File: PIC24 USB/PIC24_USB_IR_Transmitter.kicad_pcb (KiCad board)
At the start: 2 copper layers, 18 parts, among them CON1 USB-MINI-B, U1 PIC24FJXXXGB106, X1 12Mhz

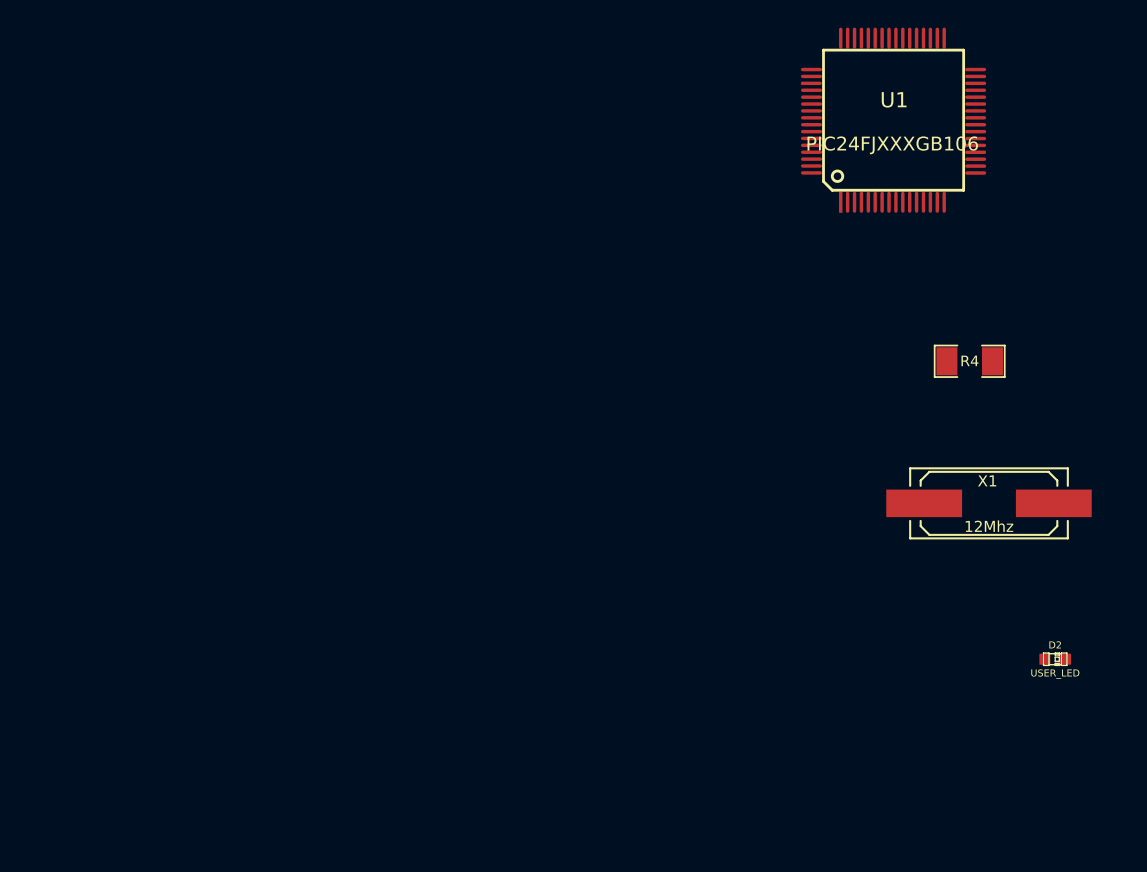
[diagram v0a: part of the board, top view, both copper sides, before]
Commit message: inserted regulator for +3v3
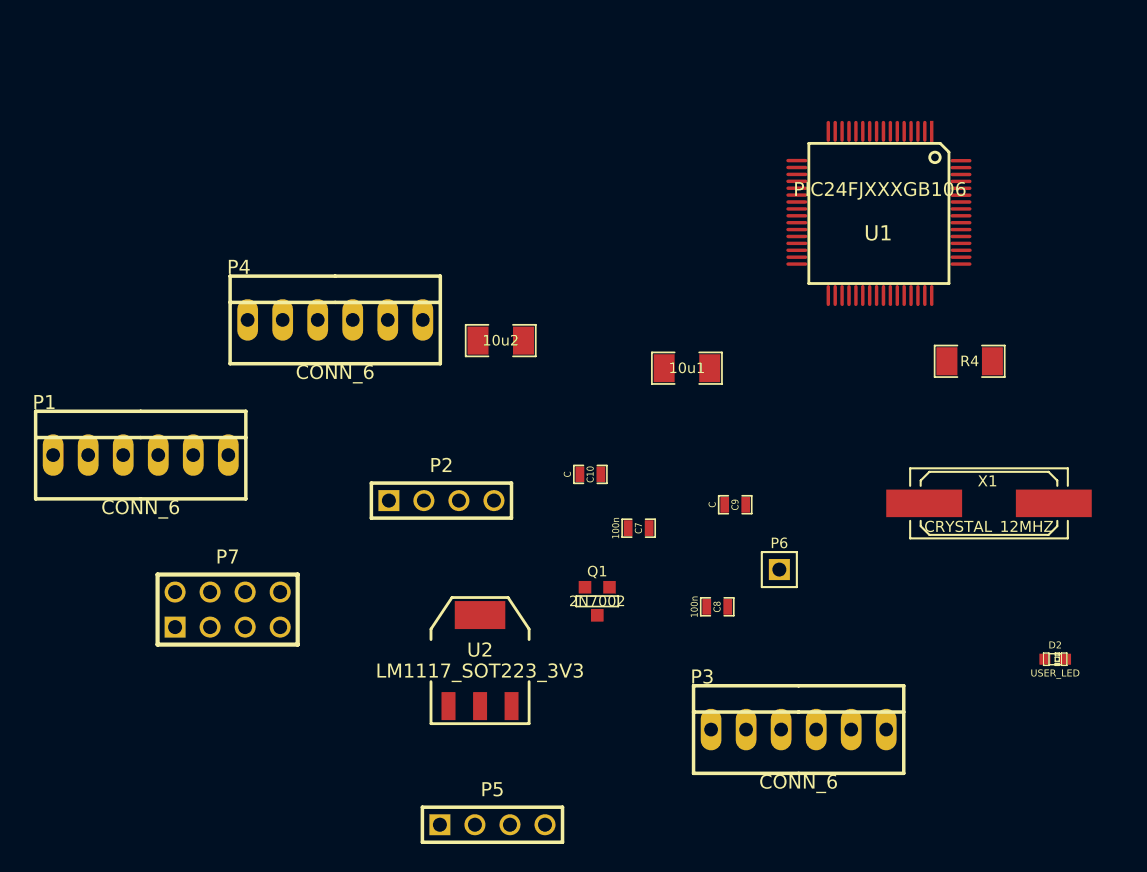
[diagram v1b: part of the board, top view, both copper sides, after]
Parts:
- added 10u1: C, SM1206, F.Cu at (105.8, 75.2)
- added 10u2: C, SM1206, F.Cu at (92.3, 73.2)
- added C10: C, SM0603_Capa, F.Cu at (98.8, 82.9)
- added C7: 100n, SM0603_Capa, F.Cu at (102.3, 86.8)
- added C8: 100n, SM0603_Capa, F.Cu at (108.0, 92.5)
- added C9: C, SM0603_Capa, F.Cu at (109.3, 85.1)
- added P1: CONN_6, PINHEAD1-6, F.Cu at (66.2, 81.5)
- added P2: CONN_4, PIN_ARRAY_4x1, F.Cu at (88.0, 84.8)
- added P3: CONN_6, PINHEAD1-6, F.Cu at (113.9, 101.4)
- added P4: CONN_6, PINHEAD1-6, F.Cu at (80.3, 71.7)
- added P5: CONN_4, PIN_ARRAY_4x1, F.Cu at (91.7, 108.3)
- added P6: CONN_1, PIN_ARRAY_1, F.Cu at (112.5, 89.8)
- added P7: CONN_8, pin_array_4x2, F.Cu at (72.5, 92.7)
- added Q1: 2N7002, SOT23GDS, F.Cu at (99.3, 92.1)
- added U2: LM1117_SOT223_3V3, SOT223, F.Cu at (90.8, 96.4)
- C3, C4: value 22p -> 100n
- X1: value 12Mhz -> CRYSTAL_12MHZ
- moved U1 6.66 mm to (119.8, 63.9), turned to 180 degrees
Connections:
- C3 pad 1: /OSC2 -> GND
- C3 pad 2: GND -> +3.3V
- C4 pad 1: /OSC1 -> GND
- C4 pad 2: GND -> +3.3V
- U1 pad 39: (no net) -> N-0000070
- U1 pad 40: (no net) -> N-0000069
- U1 pad 56: (no net) -> N-0000042
- U1 pad 57: (no net) -> +3.3V
- U1 pad 7: (no net) -> ~MCLR~
- X1 pad 1: /OSC1 -> N-0000069
- X1 pad 2: /OSC2 -> N-0000070

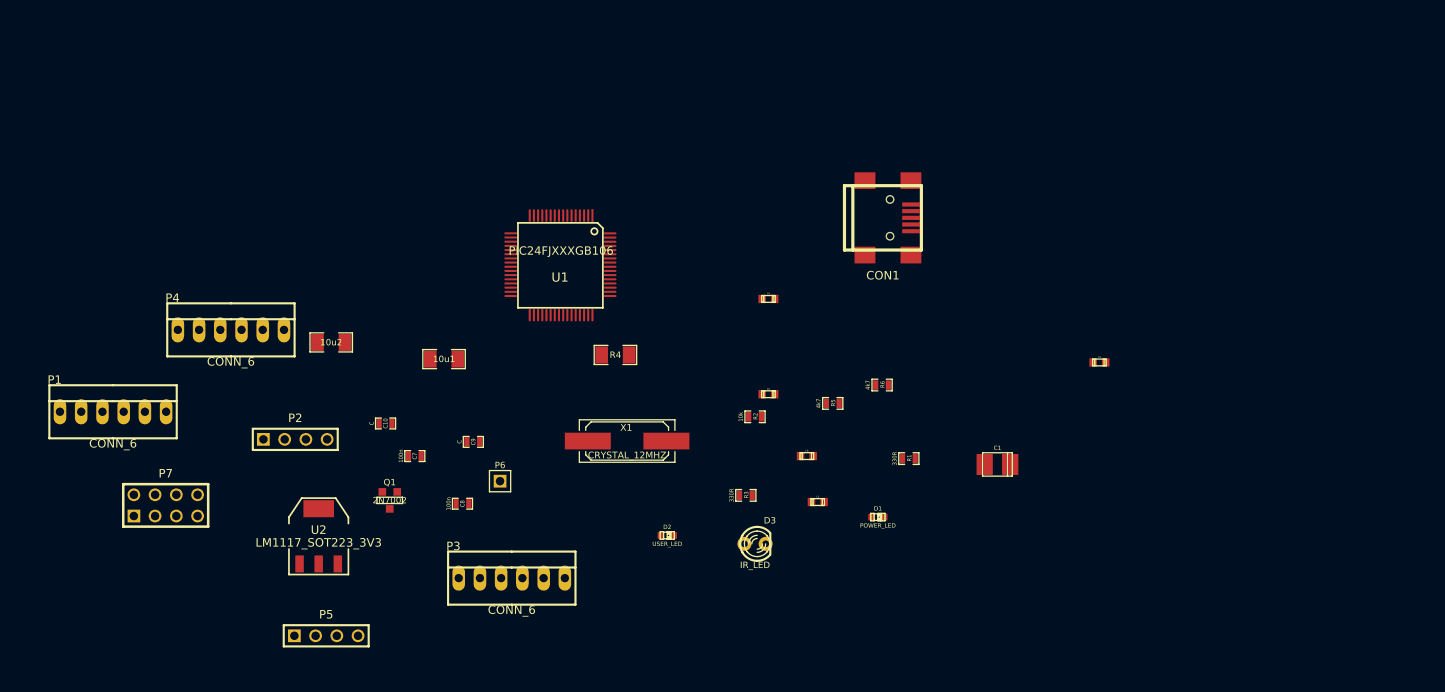
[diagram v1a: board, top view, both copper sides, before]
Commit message: inserted some mandatory mcu connecrtion and a bus connection
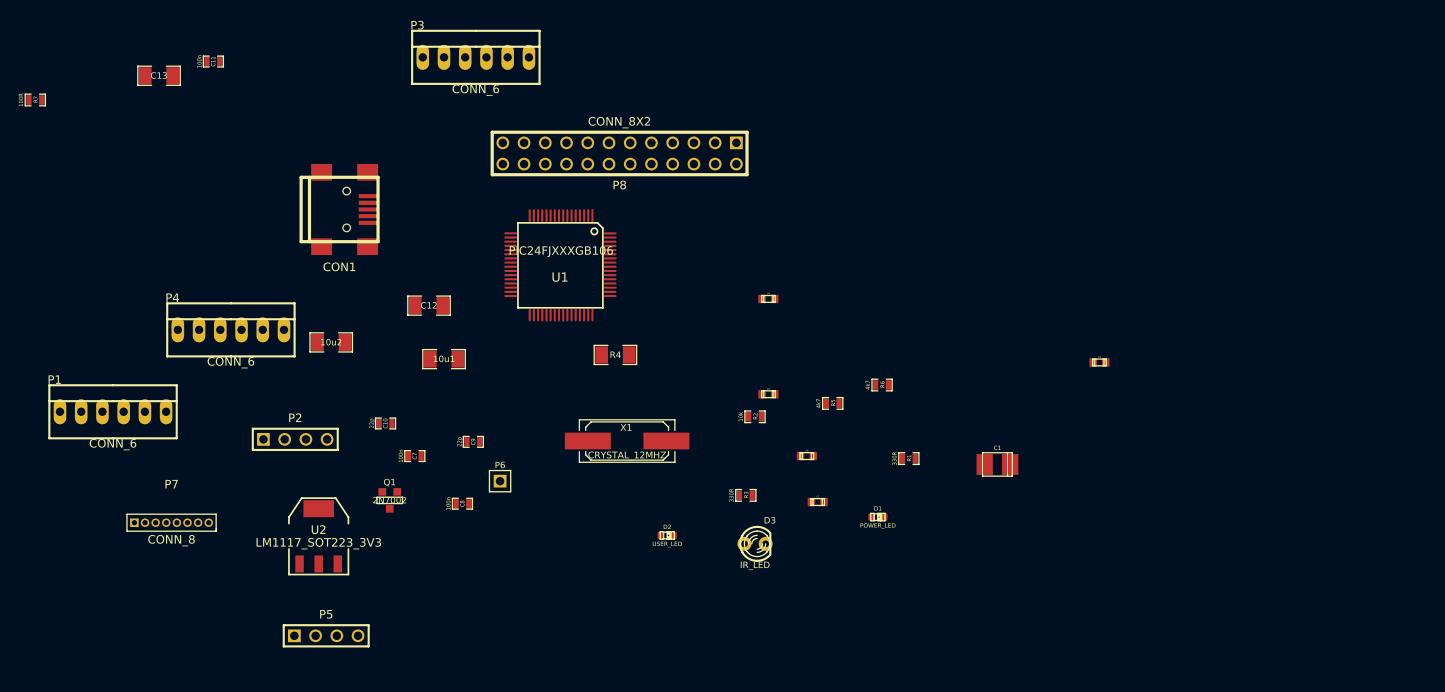
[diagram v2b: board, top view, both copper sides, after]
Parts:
- added C11: 100n, SM0603_Capa, F.Cu at (78.2, 39.6)
- added C12: 10u, SM1206, F.Cu at (104.0, 68.8)
- added C13: 10u, SM1206, F.Cu at (71.7, 41.3)
- added P8: CONN_8X2, pin_array_12x2, F.Cu at (126.8, 50.6)
- added R7: 100R, SM0603_Resistor, F.Cu at (56.9, 44.2)
- C10, C9: value C -> 22p
- P7: footprint pin_array_4x2 -> pin_array_8_50mil
- moved CON1 65.0 mm to (93.3, 57.3)
- moved P3 62.4 mm to (109.6, 39.1)
- moved P7 1.06 mm to (73.2, 93.5)
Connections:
- 10u2 pad 2: N-0000042 (its old number) -> N-0000050
- P1 pad 2: +5V -> +3.3V
- P1 pad 4: (no net) -> PGD
- P1 pad 5: (no net) -> PGC
- R2 pad 1: +5V -> ~MCLR~
- R2 pad 2: ~MCLR~ -> +3.3V
- U1 pad 1: (no net) -> /RE5
- U1 pad 17: (no net) -> PGC
- U1 pad 18: (no net) -> PGD
- U1 pad 2: (no net) -> /RE6
- U1 pad 3: (no net) -> /RE7
- U1 pad 43: (no net) -> SDA
- U1 pad 44: (no net) -> SCL
- U1 pad 56: N-0000042 (its old number) -> N-0000066
- U1 pad 60: (no net) -> /RE0
- U1 pad 61: (no net) -> /RE1
- U1 pad 62: (no net) -> /RE2
- U1 pad 63: (no net) -> /RE3
- U1 pad 64: (no net) -> /RE4
- U1 pad 7: ~MCLR~ -> N-0000072

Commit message: converted kicad project for newer version from kicad.nosoftware.cz
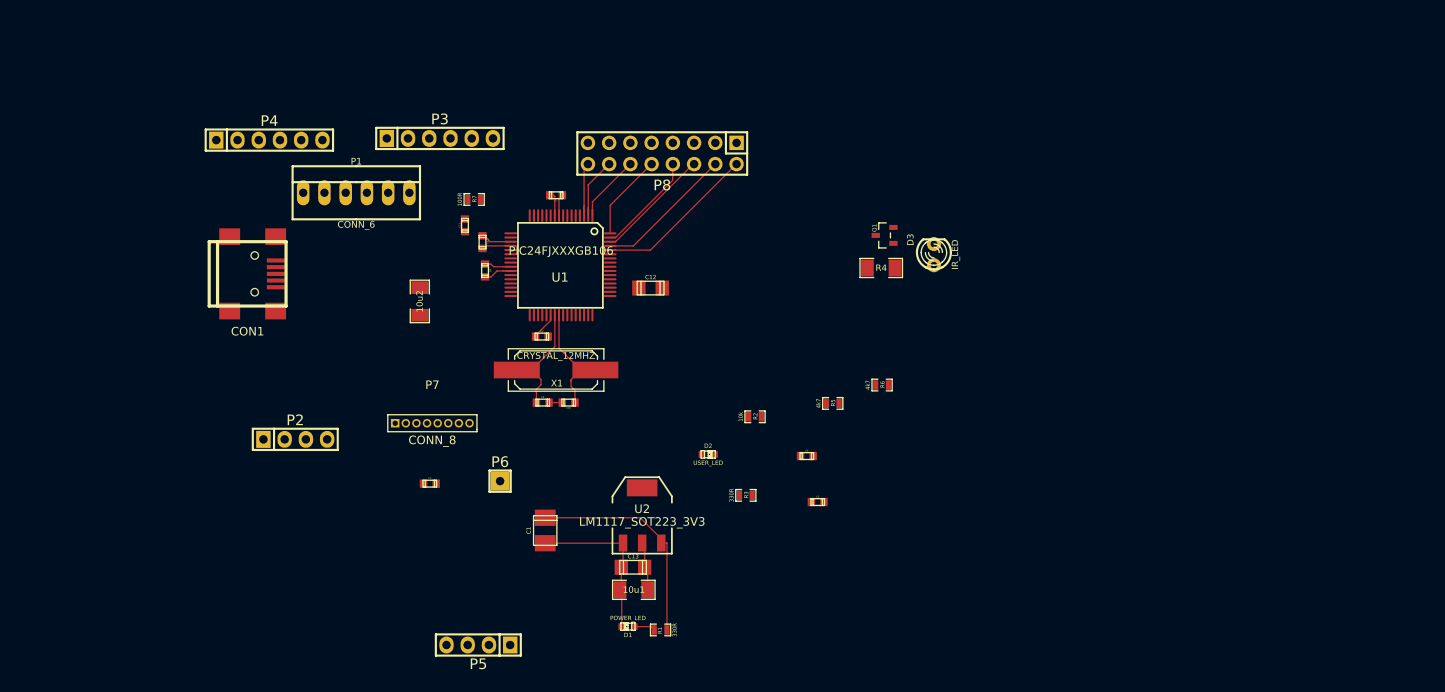
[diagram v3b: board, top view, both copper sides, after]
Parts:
- C10, C11, C7, C8, C9: footprint SM0603_Capa -> Capacitors_SMD:c_0603
- C12, C13: footprint SM1206 -> Capacitors_SMD:c_1206
- C2, C3, C4, C5, C6: footprint c_0603 -> Capacitors_SMD:c_0603
- CON1: footprint USB_MINI_B -> Connect:USB_MINI_B
- D1, D2: footprint LED-0603 -> LEDs:LED-0603
- D3: footprint LED-3MM -> LEDs:LED-3MM
- P1: footprint PINHEAD1-6 -> Connect:PINHEAD1-6
- P2, P5: footprint PIN_ARRAY_4x1 -> Pin_Headers:Pin_Header_Straight_1x04
- P3, P4: footprint PINHEAD1-6 -> Pin_Headers:Pin_Header_Straight_1x06
- P6: footprint PIN_ARRAY_1 -> Pin_Headers:Pin_Header_Straight_1x01
- P8: footprint pin_array_12x2 -> Pin_Headers:Pin_Header_Straight_2x08
- Q1: footprint SOT23GDS -> Transistors_SMD:sot23
- R1, R2, R3, R5, R6, R7: footprint SM0603_Resistor -> SMD_Packages:SM0603_Resistor
- R4: footprint SM1206 -> SMD_Packages:SM1206
- U1: footprint TQFP_64 -> SMD_Packages:TQFP_64
- U2: footprint SOT223 -> SMD_Packages:SOT223
- X1: footprint Q_49U3HMS -> Crystals_Oscillators_SMD:Q_49U3HMS
- moved C13 81.7 mm to (128.4, 100.1)
- moved Q1 67.2 mm to (158.5, 60.4), turned to 90 degrees
- moved C3 66.8 mm to (117.5, 72.5)
- moved C1 54.7 mm to (117.9, 95.7), turned to 90 degrees
- moved R7 53.8 mm to (109.4, 56.1)
- moved C5 41.9 mm to (104.1, 90.1)
- moved D3 40.7 mm to (164.4, 62.7), turned to 90 degrees
- moved P1 39.2 mm to (95.3, 55.3)
- moved U2 38.8 mm to (129.5, 93.9)
- moved R1 36.1 mm to (131.7, 107.6), turned to 180 degrees
- moved C11 35.9 mm to (108.3, 59.2), turned to 90 degrees
- moved 10u1 35.7 mm to (128.5, 102.8), turned to 180 degrees
- moved C7 35.5 mm to (119.2, 55.6), turned to 180 degrees
- moved C4 34.9 mm to (110.4, 61.2), turned to 270 degrees
- moved R4 33.5 mm to (158.1, 64.3)
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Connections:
- CON1 pad 2: (no net) -> D-
- CON1 pad 3: (no net) -> D+
- CON1 pad 4: (no net) -> Net-(CON1-Pad4)
- D3 pad 2: N-0000047 -> Net-(D3-Pad2)
- P1 pad 6: (no net) -> Net-(P1-Pad6)
- P3 pad 2: (no net) -> P1D
- P3 pad 3: (no net) -> P1C
- P3 pad 4: (no net) -> P1B
- P3 pad 5: (no net) -> P1A
- P4 pad 2: (no net) -> /AN3
- P4 pad 3: (no net) -> /AN2
- P4 pad 4: (no net) -> /AN1
- P4 pad 5: (no net) -> /AN0
- P5 pad 2: (no net) -> /RX
- P5 pad 3: (no net) -> /TX
- P7 pad 2: (no net) -> Net-(P7-Pad2)
- P7 pad 3: (no net) -> Net-(P7-Pad3)
- P7 pad 8: (no net) -> ~LCD_RESET~
- P8 pad 1: (no net) -> Net-(P8-Pad1)
- P8 pad 11: (no net) -> Net-(P8-Pad11)
- P8 pad 13: (no net) -> Net-(P8-Pad13)
- P8 pad 15: (no net) -> Net-(P8-Pad15)
- P8 pad 3: (no net) -> Net-(P8-Pad3)
- P8 pad 5: (no net) -> Net-(P8-Pad5)
- P8 pad 7: (no net) -> Net-(P8-Pad7)
- P8 pad 9: (no net) -> Net-(P8-Pad9)
- R3 pad 1: (no net) -> /USER_LED
- U1 pad 11: (no net) -> Net-(U1-Pad11)
- U1 pad 12: (no net) -> Net-(U1-Pad12)
- U1 pad 13: (no net) -> Net-(U1-Pad13)
- U1 pad 14: (no net) -> Net-(U1-Pad14)
- U1 pad 15: (no net) -> Net-(U1-Pad15)
- U1 pad 16: (no net) -> Net-(U1-Pad16)
- U1 pad 21: (no net) -> Net-(U1-Pad21)
- U1 pad 22: (no net) -> Net-(U1-Pad22)
- U1 pad 23: (no net) -> Net-(U1-Pad23)
- U1 pad 24: (no net) -> Net-(U1-Pad24)
- U1 pad 27: (no net) -> Net-(U1-Pad27)
- U1 pad 28: (no net) -> Net-(U1-Pad28)
- U1 pad 29: (no net) -> Net-(U1-Pad29)
- U1 pad 30: (no net) -> Net-(U1-Pad30)
- U1 pad 31: (no net) -> Net-(U1-Pad31)
- U1 pad 32: (no net) -> Net-(U1-Pad32)
- U1 pad 33: (no net) -> Net-(U1-Pad33)
- U1 pad 34: (no net) -> Net-(U1-Pad34)
- U1 pad 35: (no net) -> Net-(U1-Pad35)
- U1 pad 36: (no net) -> Net-(U1-Pad36)
- U1 pad 37: (no net) -> Net-(U1-Pad37)
- U1 pad 4: (no net) -> Net-(U1-Pad4)
- U1 pad 42: (no net) -> Net-(U1-Pad42)
- U1 pad 45: (no net) -> Net-(U1-Pad45)
- U1 pad 46: (no net) -> Net-(U1-Pad46)
- U1 pad 47: (no net) -> Net-(U1-Pad47)
- U1 pad 48: (no net) -> Net-(U1-Pad48)
- U1 pad 49: (no net) -> Net-(U1-Pad49)
- U1 pad 5: (no net) -> Net-(U1-Pad5)
- U1 pad 50: (no net) -> Net-(U1-Pad50)
- U1 pad 51: (no net) -> Net-(U1-Pad51)
- U1 pad 52: (no net) -> Net-(U1-Pad52)
- U1 pad 53: (no net) -> Net-(U1-Pad53)
- U1 pad 54: (no net) -> Net-(U1-Pad54)
- U1 pad 55: (no net) -> Net-(U1-Pad55)
- U1 pad 58: (no net) -> Net-(U1-Pad58)
- U1 pad 59: (no net) -> Net-(U1-Pad59)
- U1 pad 6: (no net) -> Net-(U1-Pad6)
- U1 pad 8: (no net) -> Net-(U1-Pad8)
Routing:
- net GND: track 0.00 -> 30.3 mm
- net +5V: track 0.00 -> 26.5 mm
- net /RE0: track 0.00 -> 19.4 mm
- net +3.3V: track 0.00 -> 19.3 mm
- net /RE1: track 0.00 -> 16.6 mm
- net Net-(C10-Pad1): track 0.00 -> 14.2 mm
- net Net-(C9-Pad1): track 0.00 -> 14.1 mm
- net /RE2: track 0.00 -> 13.9 mm
- net /RE3: track 0.00 -> 12.3 mm
- net /RE4: track 0.00 -> 10.3 mm
- net /RE6: track 0.00 -> 8.19 mm
- net /RE7: track 0.00 -> 8.11 mm
- net /RE5: track 0.00 -> 8.03 mm
- net Net-(D1-Pad1): track 0.00 -> 2.55 mm
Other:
- net class Default: clearance 0.254 -> 0.15; trace_width 0.254 -> 0.15
- rule trace_clearance: 0.254 -> 0.15
- rule trace_min: 0.254 -> 0.15
